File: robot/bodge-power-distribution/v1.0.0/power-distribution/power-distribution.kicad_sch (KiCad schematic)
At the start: 4 parts

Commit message: Incomplete bodge-power-distribution schematics
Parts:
- removed F?: 30A, symbol Device:Fuse
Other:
- sheet 12v_universal_reg renamed Regulator 12v0
- sheet 3v3_5v0_reg renamed Regulator 3v3 & 5v0
- sheet Power Protection ports: added TempMon_{BATT(KNEG)}, TempMon_{BATT(KPOS)}, TempMon_{PWR}, V_{BATT(PROTECTED)}, V_{BATT}, V_{CELL}[0..5], ~{FAULT}; removed FAULT_{OD}, TempMon_{batt_kneg}, TempMon_{batt_kpos}, TempMon_{pwr}, V_{batt_protected}, V_{batt}, V_{cell}[0..5]
- sheet Regulator 12v0 ports: added PGOOD, V_{BATT(6S)}; removed PGOOD_{OD}, Vbatt_6s
- sheet Regulator 3v3 & 5v0 ports: added EN_{3v3}, EN_{5v0}, PGOOD_{3v3}, PGOOD_{5v0}; removed EN_3v3, EN_5v0, PGOOD_3v3, PGOOD_5v0
- note added: "Fuse individual sub-circuits off of V_{BATT(PROTECTED)}"

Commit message: Incomplete bodge-power-distribution schematics
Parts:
- added J1: Conn_01x02, symbol Connector_Generic:Conn_01x02
- added R3: 510k, Resistor_SMD:R_0402_1005Metric_Pad0.72x0.64mm_HandSolder, symbol Device:R_Small_US
- R1: renamed from R?; value 10k -> 510k
- gave numbers to parts that had none: 2
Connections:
- net +BATT: now also R1.2, J1.1 (Pin_1); no longer SW1.2 (B)
- net GND: now also J1.2 (Pin_2), R3.2
- net Power Protection/EN: now also SW1.2 (B), R3.1; no longer R1.1, R2.1
- net at SW1.1 (A): now also R1.1, R2.1; no longer R1.2
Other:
- sheet Power Protection ports: added none; removed TempMon_{BATT(KNEG)}, TempMon_{BATT(KPOS)}, TempMon_{PWR}
- sheet Regulator 12v0 ports: added V_{IN}; removed V_{BATT(6S)}
- sheet Regulator 3v3 & 5v0 ports: added none; removed TempMonitor
- note added: "IMU Power Supply on Breakout"
- moved on the sheet: R1, R2, SW1

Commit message: Sync
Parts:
- J1: footprint (none) -> Connector_AMASS:AMASS_XT60-M_1x02_P7.20mm_Vertical
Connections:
- net +BATT: now also J1.2 (Pin_2); no longer J1.1 (Pin_1)
- net GND: now also J1.1 (Pin_1); no longer J1.2 (Pin_2)
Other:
- sheet Regulator 12v0 ports: added PGOOD_{12v0}; removed PGOOD
- note added: "1"
- note added: "2"
- moved on the sheet: J1, R1, R2, R3, SW1

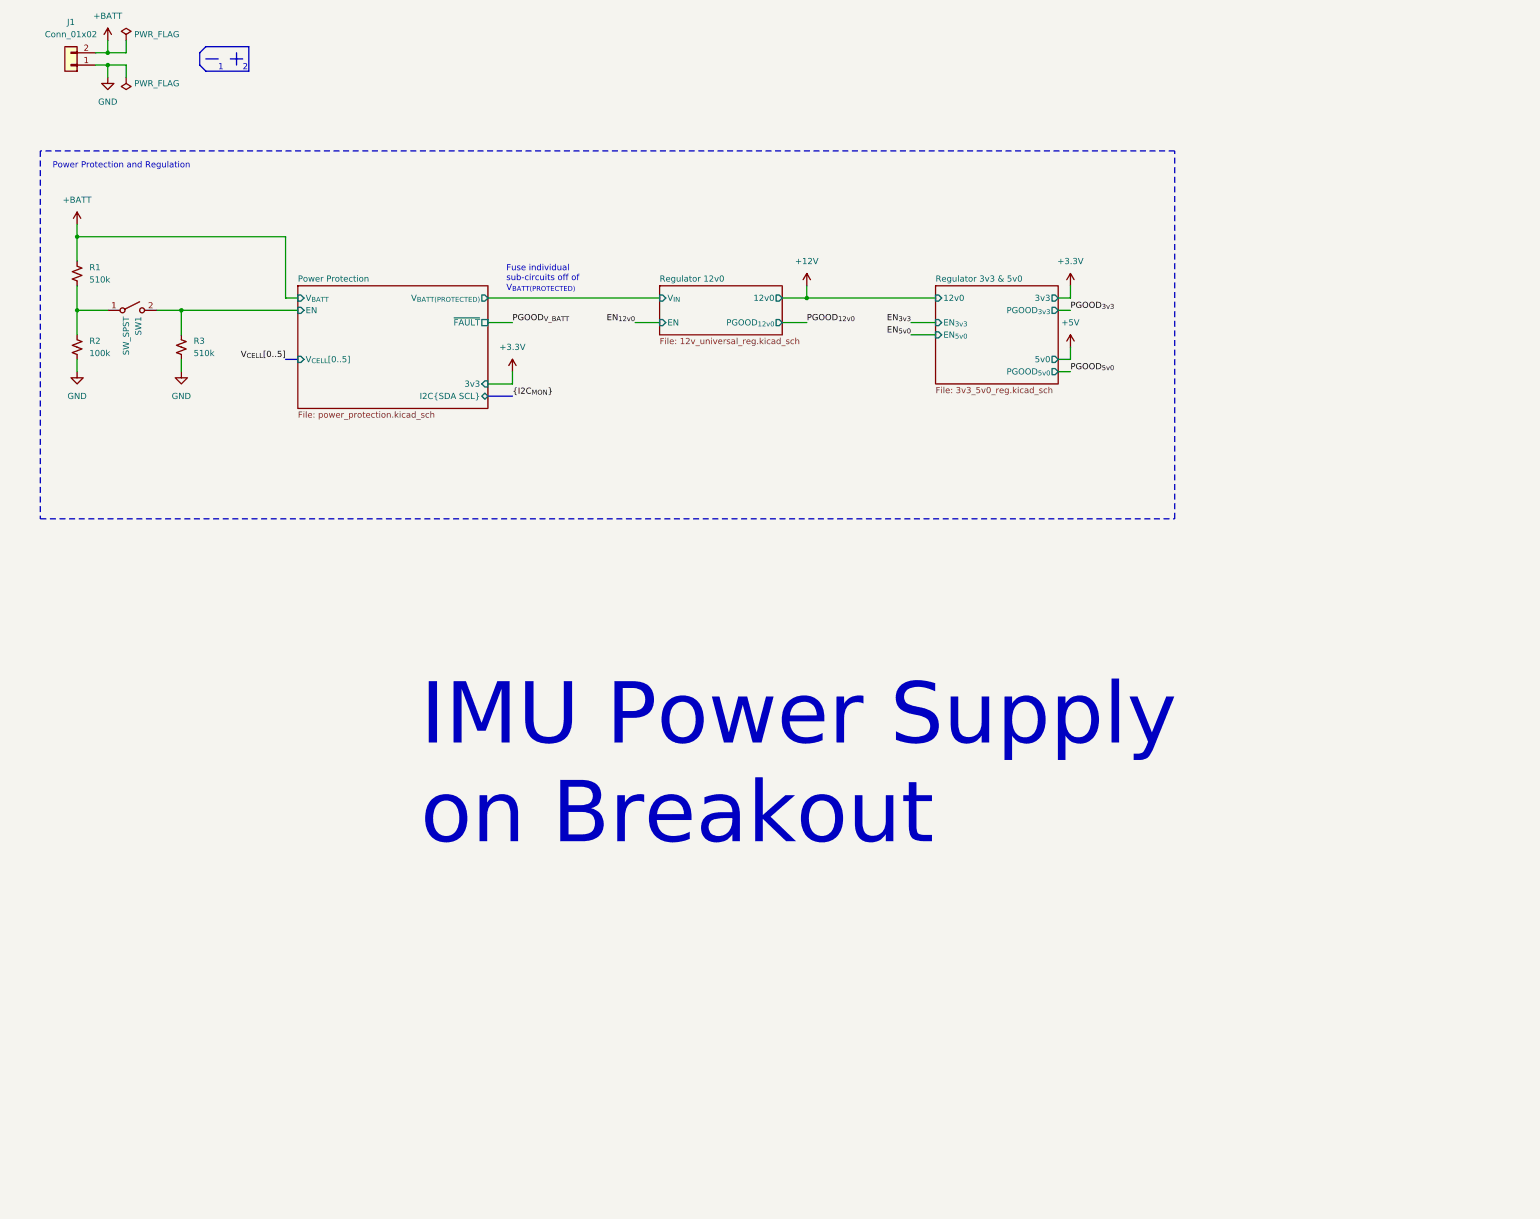
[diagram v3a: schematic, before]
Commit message: Separated power monitor into its own sheet
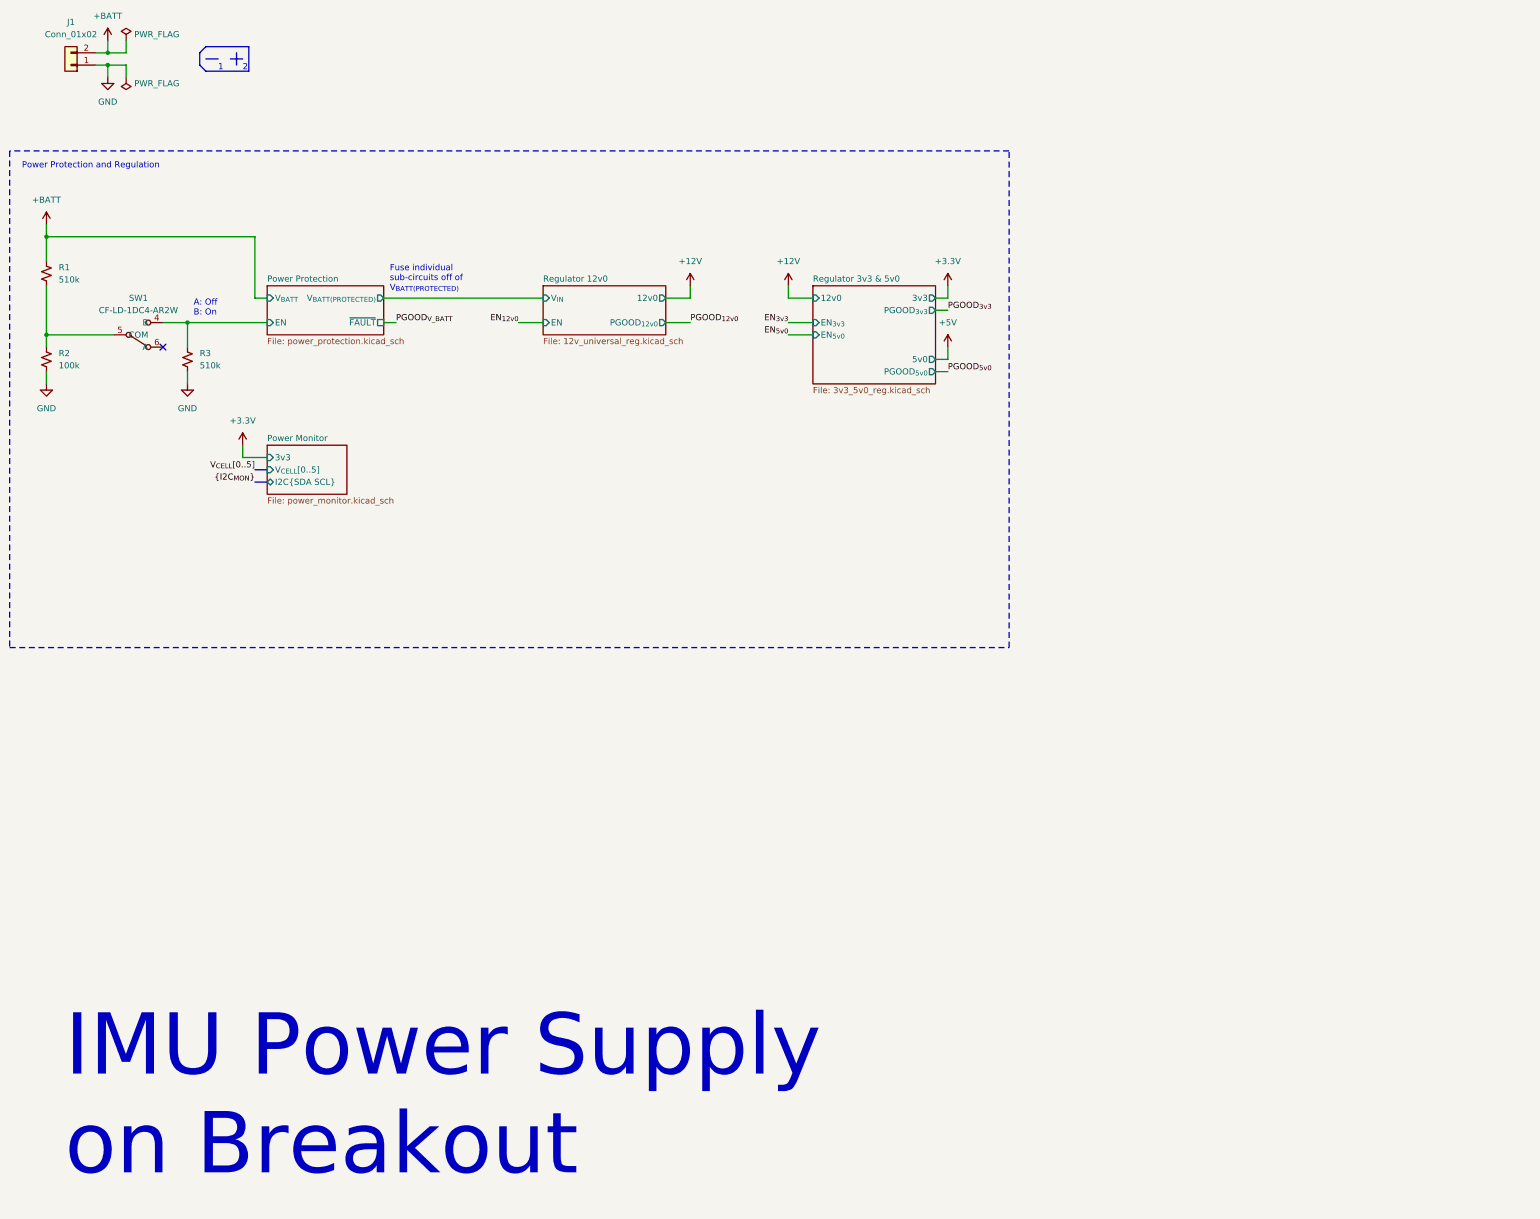
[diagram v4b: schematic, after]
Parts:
- removed SW1: SW_SPST, symbol Switch:SW_SPST
- added SW1: CF-LD-1DC4-AR2W, AT-Switches:CF-LD-1DC4-AR2W, symbol AT-Switches:SPDT_CF-LD
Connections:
- net Power Protection/EN: now also SW1.4 (B)
- net at R1.1, R2.1: now also SW1.5 (COM)
- no-connect marks 0 -> 1
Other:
- added sheet Power Monitor (power_monitor.kicad_sch)
- sheet Power Protection ports: added none; removed 3v3, I2C{SDA SCL}, V_{CELL}[0..5]
- note added: "A: Off B: On"
- moved on the sheet: R1, R2, R3

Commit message: Component updates
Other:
- note added: "~3.6V when Off ~3.1V when On"
- moved on the sheet: R1
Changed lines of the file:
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@@
   (junction (at 25.4 86.36) (diameter 0) (color 0 0 0 0)
-  )
-  (junction (at 25.4 66.04) (diameter 0) (color 0 0 0 0)
   )
   (junction (at 38.1 27.94) (diameter 0) (color 0 0 0 0)
@@
     (stroke (width 0) (type solid) (color 0 0 0 0))
   )
-  (wire (pts (xy 25.4 76.2) (xy 25.4 86.36))
+  (wire (pts (xy 25.4 83.82) (xy 25.4 86.36))
     (stroke (width 0) (type default) (color 0 0 0 0))
   )
@@
     (stroke (width 0) (type solid) (color 0 0 0 0))
   )
-  (wire (pts (xy 25.4 63.5) (xy 25.4 66.04))
+  (wire (pts (xy 25.4 76.2) (xy 25.4 78.74))
     (stroke (width 0) (type default) (color 0 0 0 0))
   )
@@
   (wire (pts (xy 41.91 25.4) (xy 41.91 27.94))
     (stroke (width 0) (type default) (color 0 0 0 0))
-  )
-  (wire (pts (xy 68.58 66.04) (xy 25.4 66.04))
-    (stroke (width 0) (type solid) (color 0 0 0 0))
   )
   (wire (pts (xy 35.56 30.48) (xy 38.1 30.48))
@@
     (stroke (width 0) (type solid) (color 0 0 0 0))
   )
-  (wire (pts (xy 68.58 78.74) (xy 68.58 66.04))
+  (wire (pts (xy 68.58 78.74) (xy 68.58 76.2))
     (stroke (width 0) (type solid) (color 0 0 0 0))
   )
@@
     (stroke (width 0) (type solid) (color 0 0 0 0))
   )
-  (wire (pts (xy 25.4 66.04) (xy 25.4 71.12))
-    (stroke (width 0) (type default) (color 0 0 0 0))
-  )
   (wire (pts (xy 179.07 83.82) (xy 184.15 83.82))
     (stroke (width 0) (type solid) (color 0 0 0 0))
@@
     (effects (font (size 1.27 1.27)) (justify left bottom))
   )
+  (text "~3.6V when Off\n~3.1V when On" (at 34.29 95.25 0)
+    (effects (font (size 1.27 1.27)) (justify left bottom))
+  )
   (text "2" (at 66.04 31.75 0)
     (effects (font (size 1.27 1.27)) (justify left bottom))
@@
     (pin "1")
   )
-  (symbol (lib_id "Device:R_Small_US") (at 25.4 73.66 180) (unit 1)
-    (in_bom yes) (on_board yes) (fields_autoplaced)
-    (property "Reference" "R1" (id 0) (at 27.94 72.3899 0)
-      (effects (font (size 1.27 1.27)) (justify right))
-    )
-    (property "Value" "510k" (id 1) (at 27.94 74.9299 0)
-      (effects (font (size 1.27 1.27)) (justify right))
-    )
-    (property "Footprint" "Resistor_SMD:R_0402_1005Metric_Pad0.72x0.64mm_HandSolder" (id 2) (at 25.4 73.66 0)
-      (effects (font (size 1.27 1.27)) hide)
-    )
-    (property "Datasheet" "~" (id 3) (at 25.4 73.66 0)
+  (symbol (lib_id "Device:R_Small_US") (at 25.4 81.28 180) (unit 1)
+    (in_bom yes) (on_board yes) (fields_autoplaced)
+    (property "Reference" "R1" (id 0) (at 27.94 80.0099 0)
+      (effects (font (size 1.27 1.27)) (justify right))
+    )
+    (property "Value" "510k" (id 1) (at 27.94 82.5499 0)
+      (effects (font (size 1.27 1.27)) (justify right))
+    )
+    (property "Footprint" "Resistor_SMD:R_0402_1005Metric_Pad0.72x0.64mm_HandSolder" (id 2) (at 25.4 81.28 0)
+      (effects (font (size 1.27 1.27)) hide)
+    )
+    (property "Datasheet" "~" (id 3) (at 25.4 81.28 0)
       (effects (font (size 1.27 1.27)) hide)
     )
@@
     (pin "1")
   )
-  (symbol (lib_id "power:+BATT") (at 25.4 63.5 0) (unit 1)
+  (symbol (lib_id "power:+BATT") (at 25.4 76.2 0) (unit 1)
     (in_bom yes) (on_board yes)
-    (property "Reference" "#PWR01" (id 0) (at 25.4 67.31 0)
-      (effects (font (size 1.27 1.27)) hide)
-    )
-    (property "Value" "+BATT" (id 1) (at 25.4 58.42 0))
-    (property "Footprint" "" (id 2) (at 25.4 63.5 0)
-      (effects (font (size 1.27 1.27)) hide)
-    )
-    (property "Datasheet" "" (id 3) (at 25.4 63.5 0)
+    (property "Reference" "#PWR01" (id 0) (at 25.4 80.01 0)
+      (effects (font (size 1.27 1.27)) hide)
+    )
+    (property "Value" "+BATT" (id 1) (at 25.4 71.12 0))
+    (property "Footprint" "" (id 2) (at 25.4 76.2 0)
+      (effects (font (size 1.27 1.27)) hide)
+    )
+    (property "Datasheet" "" (id 3) (at 25.4 76.2 0)
       (effects (font (size 1.27 1.27)) hide)
     )
@@
       (effects (font (size 1.27 1.27)) hide)
     )
-    (property "Datasheet" "" (id 3) (at 44.45 92.71 0)
+    (property "Datasheet" "https://www.digikey.com/en/products/detail/nidec-copal-electronics/CF-LD-1DC4-AR2W/6008985" (id 3) (at 44.45 92.71 0)
       (effects (font (size 1.27 1.27)) hide)
     )
@@
     (pin "5")
     (pin "6")
+  )
+  (symbol (lib_id "power:+BATT") (at 68.58 76.2 0) (unit 1)
+    (in_bom yes) (on_board yes)
+    (property "Reference" "#PWR?" (id 0) (at 68.58 80.01 0)
+      (effects (font (size 1.27 1.27)) hide)
+    )
+    (property "Value" "+BATT" (id 1) (at 68.58 71.12 0))
+    (property "Footprint" "" (id 2) (at 68.58 76.2 0)
+      (effects (font (size 1.27 1.27)) hide)
+    )
+    (property "Datasheet" "" (id 3) (at 68.58 76.2 0)
+      (effects (font (size 1.27 1.27)) hide)
+    )
+    (pin "1")
   )
   (symbol (lib_id "power:PWR_FLAG") (at 41.91 33.02 180) (unit 1)
@@
       (reference "#PWR041") (unit 1) (value "GND") (footprint "")
     )
+    (path "/7798b2a3-21c8-4d94-97ab-92817833c5e0"
+      (reference "#PWR?") (unit 1) (value "+BATT") (footprint "")
+    )
     (path "/fff34b63-f9ca-49b5-8ad5-f92410864411/c3129714-94e2-4a9d-8998-01004e940f4a"
       (reference "C1") (unit 1) (value "4.7nF") (footprint "Capacitor_SMD:C_0402_1005Metric_Pad0.74x0.62mm_HandSolder")
@@
       (reference "Q2") (unit 1) (value "SQJA80EP-T1_GE3") (footprint "Package_SO:PowerPAK_SO-8_Single")
     )
-    (path "/fe12649d-bb0a-40f3-8811-3d0e7b82a240/ef579391-6379-4520-98b5-b833eeef8a0a"
-      (reference "Q3") (unit 1) (value "SI7465DP-T1-GE3") (footprint "Package_TO_SOT_SMD:Vishay_PowerPAK_SC70-6L_Single")
+    (path "/fe12649d-bb0a-40f3-8811-3d0e7b82a240/e4f83737-aeba-4a3e-993c-e853afc84cf0"
+      (reference "Q3") (unit 1) (value "SI7465DP-T1-GE3") (footprint "Package_SO:PowerPAK_SO-8_Single")
     )
     (path "/0e56e4b6-4373-4fb5-ae59-30192de19a97"
